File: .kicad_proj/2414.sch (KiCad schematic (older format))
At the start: 1 part, among them U1 ATmega328-PU

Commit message: Finish schematics 14-16
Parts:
- added C1: 10nF, symbol Device:CP
- added C2: 100nF, symbol Device:C
- added FB1: Ferrite_Bead, symbol Device:Ferrite_Bead
- added J1: USB_B, symbol Connector:USB_B
- added U2: FT232RL, Package_SO:SSOP-28_5.3x10.2mm_P0.65mm, symbol Interface_USB:FT232RL
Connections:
- net +5V: now also FB1.1, U2.20 (VCC), U2.4 (VCCIO)
- net GND: now also C1.2, C2.2, J1.4 (GND), U2.18 (GND), U2.21 (GND), U2.25 (AGND), U2.7 (GND)
- net at U1.2 (PD0): now also U2.1 (TXD)
- net at U1.3 (PD1): now also U2.5 (RXD)
- new net: J1.3 (D+), U2.15 (USBD+)
- new net: J1.2 (D-), U2.16 (USBD-)
- new net: C2.1, U2.17 (3V3OUT)
- new net: C1.1, FB1.2, J1.1 (VBUS)
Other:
- moved on the sheet: U1
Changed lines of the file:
@@
 L MCU_Microchip_ATmega:ATmega328-PU U?
 U 1 1 60A417FE
-P 4950 3500
+P 5775 2475
 AR Path="/60A417FE" Ref="U?"  Part="1"
 AR Path="/607B2C9D/60A417FE" Ref="U1"  Part="1"
 AR Path="/60A3FFA8/60A417FE" Ref="U?"  Part="1"
 AR Path="/60A4150D/60A417FE" Ref="U?"  Part="1"
-AR Path="/60A41615/60A417FE" Ref="U?"  Part="1"
-F 0 "U?" H 4306 3546 50  0000 R CNN
-F 1 "ATmega328-PU" H 4306 3455 50  0000 R CNN
-F 2 "Package_DIP:DIP-28_W7.62mm" H 4950 3500 50  0001 C CIN
-F 3 "http://ww1.microchip.com/downloads/en/DeviceDoc/ATmega328_P%20AVR%20MCU%20with%20picoPower%20Technology%20Data%20Sheet%2040001984A.pdf" H 4950 3500 50  0001 C CNN
-	1    4950 3500
-	1    0    0    -1
+AR Path="/60A41615/60A417FE" Ref="U1"  Part="1"
+F 0 "U1" H 5225 2550 50  0000 R CNN
+F 1 "ATmega328-PU" H 5225 2450 50  0000 R CNN
+F 2 "Package_DIP:DIP-28_W7.62mm" H 5775 2475 50  0001 C CIN
+F 3 "http://ww1.microchip.com/downloads/en/DeviceDoc/ATmega328_P%20AVR%20MCU%20with%20picoPower%20Technology%20Data%20Sheet%2040001984A.pdf" H 5775 2475 50  0001 C CNN
+	1    5775 2475
+	-1   0    0    1
 $EndComp
 $Comp
 L power:GND #PWR?
 U 1 1 60A417FA
-P 4950 5000
+P 4825 4375
 AR Path="/60A417FA" Ref="#PWR?"  Part="1"
 AR Path="/607B2C9D/60A417FA" Ref="#PWR?"  Part="1"
@@
 AR Path="/60A4150D/60A417FA" Ref="#PWR?"  Part="1"
 AR Path="/60A41615/60A417FA" Ref="#PWR?"  Part="1"
-F 0 "#PWR?" H 4950 4750 50  0001 C CNN
-F 1 "GND" H 4955 4827 50  0000 C CNN
-F 2 "" H 4950 5000 50  0001 C CNN
-F 3 "" H 4950 5000 50  0001 C CNN
-	1    4950 5000
+F 0 "#PWR?" H 4825 4125 50  0001 C CNN
+F 1 "GND" H 4830 4202 50  0000 C CNN
+F 2 "" H 4825 4375 50  0001 C CNN
+F 3 "" H 4825 4375 50  0001 C CNN
+	1    4825 4375
+	1    0    0    -1
+$EndComp
+$Comp
+L Interface_USB:FT232RL U2
+U 1 1 60B487A5
+P 3550 2475
+F 0 "U2" H 3750 3500 50  0000 C CNN
+F 1 "FT232RL" H 3875 3400 50  0000 C CNN
+F 2 "Package_SO:SSOP-28_5.3x10.2mm_P0.65mm" H 4650 1575 50  0001 C CNN
+F 3 "https://www.ftdichip.com/Support/Documents/DataSheets/ICs/DS_FT232R.pdf" H 3550 2475 50  0001 C CNN
+	1    3550 2475
 	1    0    0    -1
 $EndComp
@@
 L power:+5V #PWR?
 U 1 1 60A417FC
-P 4950 2000
+P 2625 1075
 AR Path="/60A417FC" Ref="#PWR?"  Part="1"
 AR Path="/607B2C9D/60A417FC" Ref="#PWR?"  Part="1"
@@
 AR Path="/60A4150D/60A417FC" Ref="#PWR?"  Part="1"
 AR Path="/60A41615/60A417FC" Ref="#PWR?"  Part="1"
-F 0 "#PWR?" H 4950 1850 50  0001 C CNN
-F 1 "+5V" H 4965 2173 50  0000 C CNN
-F 2 "" H 4950 2000 50  0001 C CNN
-F 3 "" H 4950 2000 50  0001 C CNN
-	1    4950 2000
+F 0 "#PWR?" H 2625 925 50  0001 C CNN
+F 1 "+5V" H 2640 1248 50  0000 C CNN
+F 2 "" H 2625 1075 50  0001 C CNN
+F 3 "" H 2625 1075 50  0001 C CNN
+	1    2625 1075
 	1    0    0    -1
 $EndComp
+Wire Wire Line
+	4350 1775 4775 1775
+Wire Wire Line
+	4775 1975 5175 1975
+Wire Wire Line
+	4775 1775 4775 1975
+Wire Wire Line
+	4350 1875 5175 1875
+Wire Wire Line
+	4825 4375 4825 4275
+Wire Wire Line
+	5775 925  5775 975
+Wire Wire Line
+	4825 4275 3750 4275
+Wire Wire Line
+	3750 4275 3750 3575
+Connection ~ 4825 4275
+Wire Wire Line
+	3650 3475 3650 3575
+Wire Wire Line
+	3650 3575 3750 3575
+Connection ~ 3750 3575
+Wire Wire Line
+	3750 3575 3750 3475
+Wire Wire Line
+	3650 3575 3550 3575
+Wire Wire Line
+	3350 3575 3350 3475
+Connection ~ 3650 3575
+Wire Wire Line
+	3550 3475 3550 3575
+Connection ~ 3550 3575
+Wire Wire Line
+	3550 3575 3350 3575
+Wire Wire Line
+	3650 1475 3650 1175
+Wire Wire Line
+	3650 1175 3450 1175
+Wire Wire Line
+	3450 1475 3450 1175
+Connection ~ 3450 1175
+Wire Wire Line
+	3450 1175 2625 1175
+$Comp
+L Connector:USB_B J1
+U 1 1 60B801EF
+P 1825 2075
+F 0 "J1" H 1882 2542 50  0000 C CNN
+F 1 "USB_B" H 1882 2451 50  0000 C CNN
+F 2 "" H 1975 2025 50  0001 C CNN
+F 3 " ~" H 1975 2025 50  0001 C CNN
+	1    1825 2075
+	1    0    0    -1
+$EndComp
+$Comp
+L Device:Ferrite_Bead FB1
+U 1 1 60B831C7
+P 2625 1400
+F 0 "FB1" H 2762 1446 50  0000 L CNN
+F 1 "Ferrite_Bead" H 2762 1355 50  0000 L CNN
+F 2 "" V 2555 1400 50  0001 C CNN
+F 3 "~" H 2625 1400 50  0001 C CNN
+	1    2625 1400
+	1    0    0    -1
+$EndComp
+Wire Wire Line
+	2625 1075 2625 1175
+Connection ~ 2625 1175
+Wire Wire Line
+	2625 1175 2625 1250
+Wire Wire Line
+	2625 1550 2375 1550
+Wire Wire Line
+	2125 1550 2125 1875
+Wire Wire Line
+	3350 3575 2375 3575
+Wire Wire Line
+	1825 3575 1825 2475
+Connection ~ 3350 3575
+$Comp
+L Device:C C2
+U 1 1 60B856CC
+P 2700 3825
+F 0 "C2" H 2815 3871 50  0000 L CNN
+F 1 "100nF" H 2815 3780 50  0000 L CNN
+F 2 "" H 2738 3675 50  0001 C CNN
+F 3 "~" H 2700 3825 50  0001 C CNN
+	1    2700 3825
+	1    0    0    -1
+$EndComp
+Wire Wire Line
+	2375 2400 2375 1550
+Connection ~ 2375 1550
+Wire Wire Line
+	2375 1550 2125 1550
+Wire Wire Line
+	2375 2700 2375 3575
+Connection ~ 2375 3575
+Wire Wire Line
+	2375 3575 1825 3575
+$Comp
+L Device:CP C1
+U 1 1 60B8A756
+P 2375 2550
+F 0 "C1" H 2493 2596 50  0000 L CNN
+F 1 "10nF" H 2493 2505 50  0000 L CNN
+F 2 "" H 2413 2400 50  0001 C CNN
+F 3 "~" H 2375 2550 50  0001 C CNN
+	1    2375 2550
+	1    0    0    -1
+$EndComp
+Wire Wire Line
+	2750 2075 2125 2075
+Wire Wire Line
+	2125 2175 2750 2175
+Wire Wire Line
+	2750 1775 2700 1775
+Wire Wire Line
+	2700 1775 2700 3675
+Wire Wire Line
+	2700 3975 2700 4275
+Wire Wire Line
+	2700 4275 3750 4275
+Connection ~ 3750 4275
+Wire Wire Line
+	3650 1175 4925 1175
+Connection ~ 3650 1175
+Wire Wire Line
+	4825 4275 5000 4275
+Wire Wire Line
+	4925 1175 4925 4050
+Wire Wire Line
+	4925 4050 5775 4050
+Wire Wire Line
+	5775 4050 5775 3975
+Wire Wire Line
+	5000 4275 5000 925
+Wire Wire Line
+	5000 925  5775 925
 $EndSCHEMATC

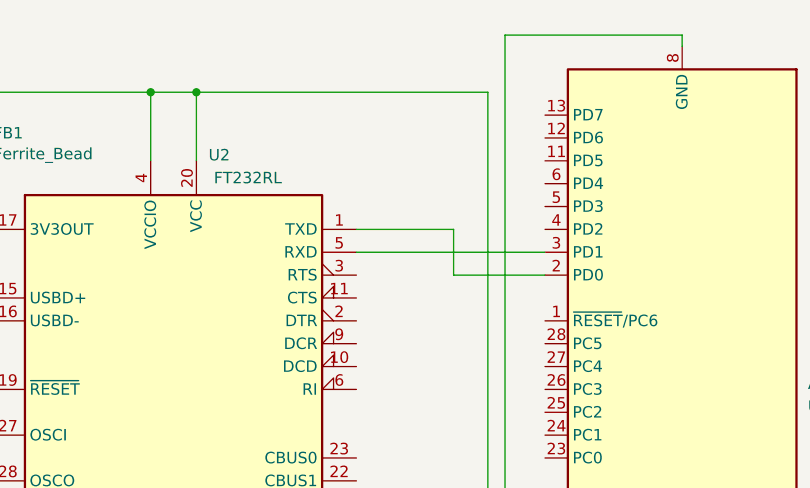
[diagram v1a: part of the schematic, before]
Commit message: Add resistors
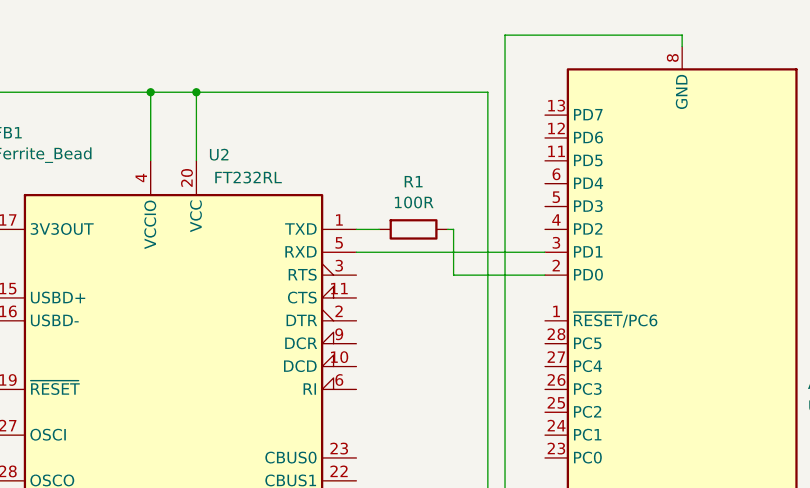
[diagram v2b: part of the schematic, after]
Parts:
- added R1: 100R, symbol Device:R
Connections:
- net at U1.2 (PD0): now also R1.1; no longer U2.1 (TXD)
- new net: R1.2, U2.1 (TXD)
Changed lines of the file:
@@
 $EndComp
 Wire Wire Line
-	4350 1775 4775 1775
-Wire Wire Line
 	4775 1975 5175 1975
-Wire Wire Line
-	4775 1775 4775 1975
 Wire Wire Line
 	4350 1875 5175 1875
@@
 Wire Wire Line
 	5000 925  5775 925
+$Comp
+L Device:R R1
+U 1 1 60D4DD8A
+P 4600 1775
+F 0 "R1" V 4393 1775 50  0000 C CNN
+F 1 "100R" V 4484 1775 50  0000 C CNN
+F 2 "" V 4530 1775 50  0001 C CNN
+F 3 "~" H 4600 1775 50  0001 C CNN
+	1    4600 1775
+	0    1    1    0
+$EndComp
+Wire Wire Line
+	4750 1775 4775 1775
+Wire Wire Line
+	4775 1775 4775 1975
+Wire Wire Line
+	4450 1775 4350 1775
 $EndSCHEMATC
